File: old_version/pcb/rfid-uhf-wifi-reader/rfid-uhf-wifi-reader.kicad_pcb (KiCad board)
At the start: 2 copper layers, 50 x 50 mm, 23 parts, among them J1 USB_OTG, J2 Conn_01x05, Q1 BSS138, Q2 BSS138, SW1 SW_Push, SW2 SW_Push, U1 ESP32-WROOM-32, U2 AMS1117-3.3, U3 CH340E

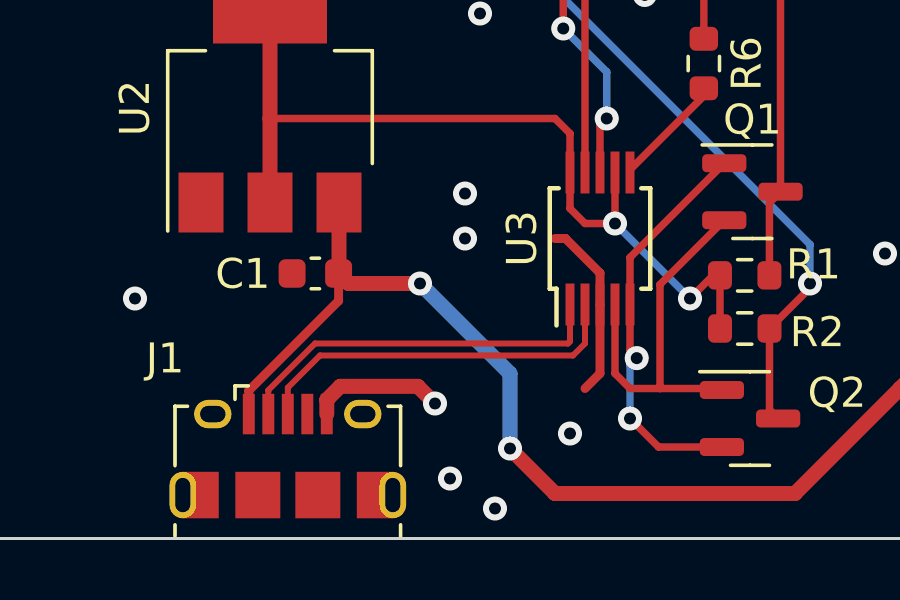
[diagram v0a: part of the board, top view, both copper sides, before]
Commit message: fix usb data inverted
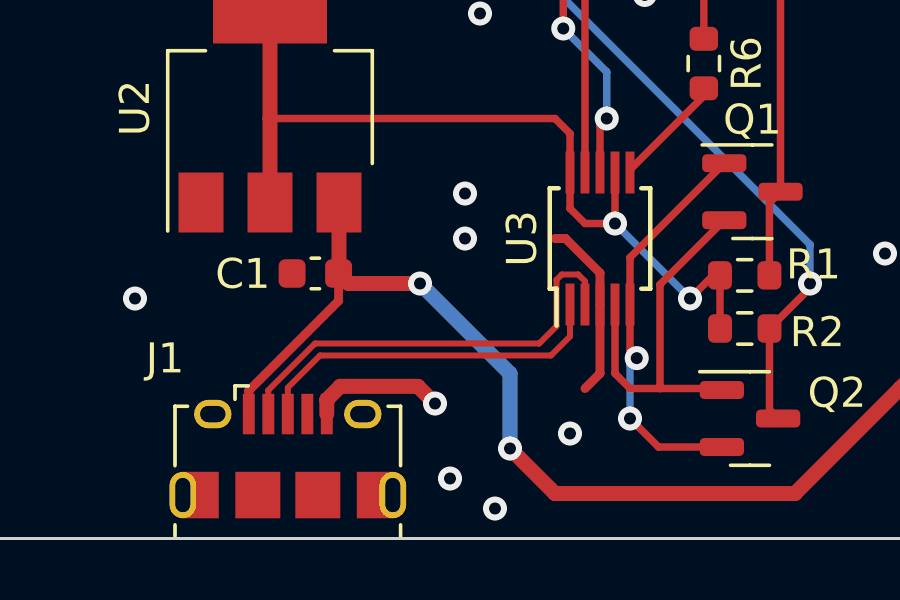
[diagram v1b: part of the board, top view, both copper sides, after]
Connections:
- U3 pad 1: D- -> D+
- U3 pad 2: D+ -> D-
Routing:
- net D-: track 12.8 -> 14.7 mm
- net D+: track 12.7 -> 12.1 mm
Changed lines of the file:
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@@
       (stroke (width 0.15) (type solid)) (layer "F.Fab"))
     (pad "1" smd rect (at -2.2 -1 90) (size 1.4 0.3) (layers "F.Cu" "F.Paste" "F.Mask")
-      (net 6 "D-") (pinfunction "UD+") (pintype "bidirectional"))
+      (net 5 "D+") (pinfunction "UD+") (pintype "bidirectional"))
     (pad "2" smd rect (at -2.2 -0.5 90) (size 1.4 0.3) (layers "F.Cu" "F.Paste" "F.Mask")
-      (net 5 "D+") (pinfunction "UD-") (pintype "bidirectional"))
+      (net 6 "D-") (pinfunction "UD-") (pintype "bidirectional"))
     (pad "3" smd rect (at -2.2 0 90) (size 1.4 0.3) (layers "F.Cu" "F.Paste" "F.Mask")
       (net 2 "GND") (pinfunction "GND") (pintype "power_in"))
@@
   (segment (start 127 49.5) (end 123 45.5) (width 0.25) (layer "B.Cu") (net 4))
   (segment (start 123 45.5) (end 121.5 45.5) (width 0.25) (layer "B.Cu") (net 4))
-  (segment (start 124.5 83.5) (end 124.5 82.2) (width 0.2) (layer "F.Cu") (net 5))
-  (segment (start 115.665486 83.89952) (end 124.10048 83.89952) (width 0.2) (layer "F.Cu") (net 5))
+  (segment (start 124 83.264) (end 124 82.2) (width 0.2) (layer "F.Cu") (net 5))
+  (segment (start 115.665486 83.89952) (end 123.36448 83.89952) (width 0.2) (layer "F.Cu") (net 5))
+  (segment (start 114.593254 85.852051) (end 114.593254 84.971752) (width 0.2) (layer "F.Cu") (net 5))
+  (segment (start 123.36448 83.89952) (end 124 83.264) (width 0.2) (layer "F.Cu") (net 5))
   (segment (start 114.593254 84.971752) (end 115.665486 83.89952) (width 0.2) (layer "F.Cu") (net 5))
-  (segment (start 114.593254 85.852051) (end 114.593254 84.971752) (width 0.2) (layer "F.Cu") (net 5))
-  (segment (start 124.10048 83.89952) (end 124.5 83.5) (width 0.2) (layer "F.Cu") (net 5))
+  (segment (start 113.943254 85.852051) (end 113.943254 85.056746) (width 0.2) (layer "F.Cu") (net 6))
+  (segment (start 124.5 81.425736) (end 124.5 82.2) (width 0.2) (layer "F.Cu") (net 6))
+  (segment (start 123.55 81.375736) (end 123.725736 81.2) (width 0.2) (layer "F.Cu") (net 6))
+  (segment (start 123.725736 81.2) (end 124.274264 81.2) (width 0.2) (layer "F.Cu") (net 6))
   (segment (start 113.943254 85.056746) (end 115.5 83.5) (width 0.2) (layer "F.Cu") (net 6))
-  (segment (start 124 83.434994) (end 124 82.2) (width 0.2) (layer "F.Cu") (net 6))
-  (segment (start 123.934994 83.5) (end 124 83.434994) (width 0.2) (layer "F.Cu") (net 6))
-  (segment (start 113.943254 85.852051) (end 113.943254 85.056746) (width 0.2) (layer "F.Cu") (net 6))
-  (segment (start 115.5 83.5) (end 123.934994 83.5) (width 0.2) (layer "F.Cu") (net 6))
+  (segment (start 124.274264 81.2) (end 124.5 81.425736) (width 0.2) (layer "F.Cu") (net 6))
+  (segment (start 122.973157 83.5) (end 123.55 82.923157) (width 0.2) (layer "F.Cu") (net 6))
+  (segment (start 123.55 82.923157) (end 123.55 81.375736) (width 0.2) (layer "F.Cu") (net 6))
+  (segment (start 115.5 83.5) (end 122.973157 83.5) (width 0.2) (layer "F.Cu") (net 6))
   (segment (start 95.175 54) (end 93.2875 54) (width 0.25) (layer "F.Cu") (net 7))
   (segment (start 95.175 49.5) (end 93.2875 49.5) (width 0.25) (layer "F.Cu") (net 8))
